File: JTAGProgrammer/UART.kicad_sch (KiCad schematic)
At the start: 25 parts, among them J3 Conn_01x06, U6 74LVC3G17, U7 74LVC3G17

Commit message: Add LCSC part numbers
Signed-off-by: Anthony Bernaert <anthony.bernaert@gmail.com>
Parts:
- D1: LCSC (none) -> C142698
- D4: LCSC (none) -> C324473
- J3: LCSC (none) -> C40877
- U6, U7: LCSC (none) -> C18213
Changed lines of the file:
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@@
+      (effects (font (size 1.27 1.27)) hide)
+    )
+    (property "LCSC" "C18213" (at 41.275 170.18 0)
       (effects (font (size 1.27 1.27)) hide)
     )
@@
       (effects (font (size 1.27 1.27)) (justify bottom) hide)
     )
+    (property "LCSC" "C142698" (at 197.485 87.63 90)
+      (effects (font (size 1.27 1.27)) hide)
+    )
     (pin "1")
     (pin "2")
@@
     )
     (property "Datasheet" "http://www.ti.com/lit/sg/scyt129e/scyt129e.pdf" (at 127.635 41.275 0)
+      (effects (font (size 1.27 1.27)) hide)
+    )
+    (property "LCSC" "C18213" (at 127.635 41.275 0)
       (effects (font (size 1.27 1.27)) hide)
     )
@@
       (effects (font (size 1.27 1.27)) hide)
     )
+    (property "LCSC" "C18213" (at 127.635 74.93 0)
+      (effects (font (size 1.27 1.27)) hide)
+    )
     (pin "1")
     (pin "7")
@@
       (effects (font (size 1.27 1.27)) hide)
     )
+    (property "LCSC" "C18213" (at 209.55 121.92 0)
+      (effects (font (size 1.27 1.27)) hide)
+    )
     (pin "1")
     (pin "7")
@@
       (effects (font (size 1.27 1.27)) hide)
     )
+    (property "LCSC" "C324473" (at 57.15 133.35 0)
+      (effects (font (size 1.27 1.27)) hide)
+    )
     (pin "1")
     (pin "2")
@@
     )
     (property "Datasheet" "~" (at 247.015 77.47 0)
+      (effects (font (size 1.27 1.27)) hide)
+    )
+    (property "LCSC" "C40877" (at 247.015 77.47 0)
       (effects (font (size 1.27 1.27)) hide)
     )
@@
       (effects (font (size 1.27 1.27)) hide)
     )
+    (property "LCSC" "C324473" (at 57.15 123.19 0)
+      (effects (font (size 1.27 1.27)) hide)
+    )
     (pin "1")
     (pin "2")
@@
     )
     (property "Datasheet" "http://www.ti.com/lit/sg/scyt129e/scyt129e.pdf" (at 64.77 170.18 0)
+      (effects (font (size 1.27 1.27)) hide)
+    )
+    (property "LCSC" "C18213" (at 64.77 170.18 0)
       (effects (font (size 1.27 1.27)) hide)
     )
@@
       (effects (font (size 1.27 1.27)) hide)
     )
+    (property "LCSC" "C18213" (at 209.55 142.875 0)
+      (effects (font (size 1.27 1.27)) hide)
+    )
     (pin "1")
     (pin "7")
@@
       (effects (font (size 1.27 1.27)) (justify bottom) hide)
     )
+    (property "LCSC" "C142698" (at 210.185 87.63 90)
+      (effects (font (size 1.27 1.27)) hide)
+    )
     (pin "1")
     (pin "2")
@@
     )
     (property "Datasheet" "http://www.ti.com/lit/sg/scyt129e/scyt129e.pdf" (at 125.095 92.71 0)
+      (effects (font (size 1.27 1.27)) hide)
+    )
+    (property "LCSC" "C18213" (at 125.095 92.71 0)
       (effects (font (size 1.27 1.27)) hide)
     )
@@
       (effects (font (size 1.27 1.27)) hide)
     )
+    (property "LCSC" "C324473" (at 57.15 113.03 0)
+      (effects (font (size 1.27 1.27)) hide)
+    )
     (pin "1")
     (pin "2")
@@
       (effects (font (size 1.27 1.27)) (justify bottom) hide)
     )
+    (property "LCSC" "C142698" (at 203.835 87.63 90)
+      (effects (font (size 1.27 1.27)) hide)
+    )
     (pin "1")
     (pin "2")
@@
       (effects (font (size 1.27 1.27)) (justify bottom) hide)
     )
+    (property "LCSC" "C142698" (at 216.535 87.63 90)
+      (effects (font (size 1.27 1.27)) hide)
+    )
     (pin "1")
     (pin "2")
@@
       (effects (font (size 1.27 1.27)) hide)
     )
+    (property "LCSC" "C18213" (at 125.73 58.42 0)
+      (effects (font (size 1.27 1.27)) hide)
+    )

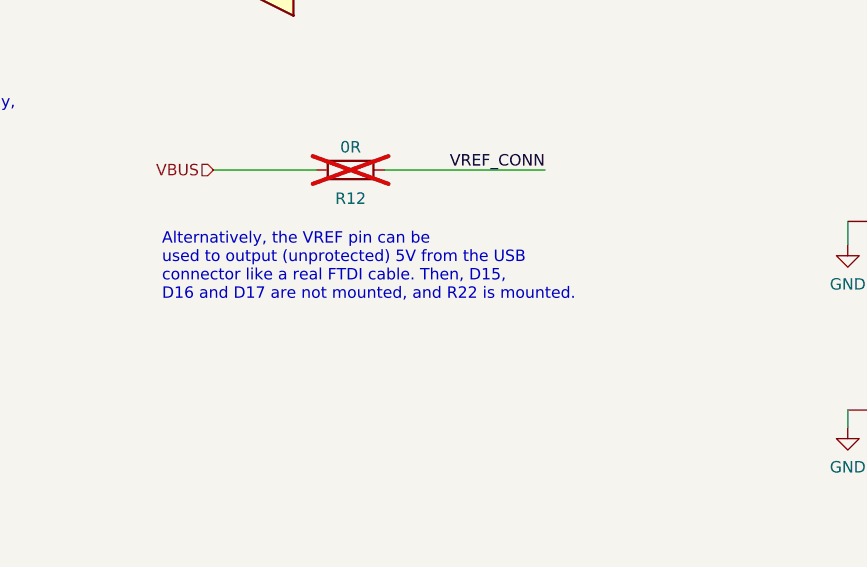
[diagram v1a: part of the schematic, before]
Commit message: Fix wrong comment in schematic on UART VREF/5V mounting options
Signed-off-by: Anthony Bernaert <anthony.bernaert@gmail.com>
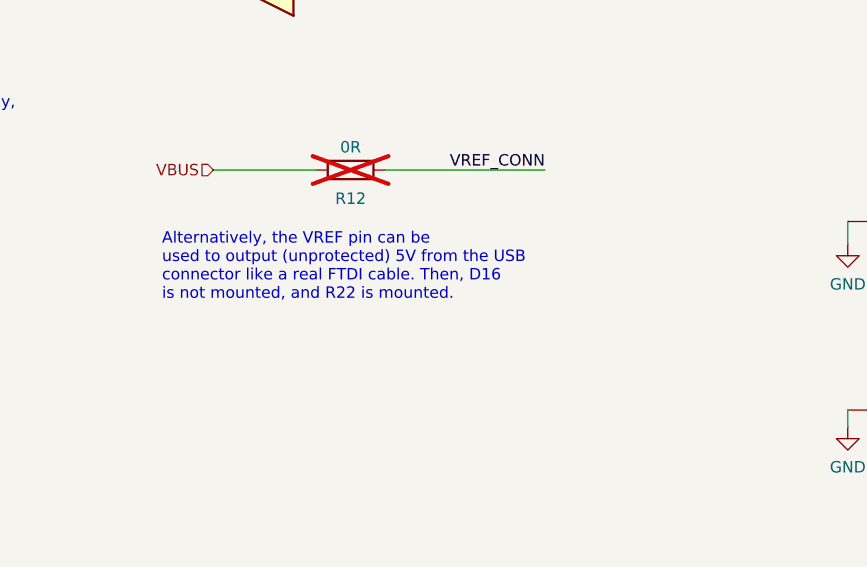
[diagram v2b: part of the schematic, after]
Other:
- note added: "Alternatively, the VREF pin can be used to output (unprotected) 5V from the USB connector like a real FTDI cable. Then, D16 is not mounted, and R22 is mounted."
- note removed: "Alternatively, the VREF pin can be used to output (unprotected) 5V from the USB connector like a real FTDI cable. Then, D15, D16 and D17 are not mounted, and R22 is mounted."
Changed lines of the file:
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@@
     (title "FTDI JTAG Programmer")
     (date "2024-10-11")
-    (rev "1")
+    (rev "1.1")
   )
   (junction (at 210.185 92.71) (diameter 0) (color 0 0 0 0)
@@
     (stroke (width 0) (type default))
   )
-  (text "Alternatively, the VREF pin can be \nused to output (unprotected) 5V from the USB\nconnector like a real FTDI cable. Then, D15,\nD16 and D17 are not mounted, and R22 is mounted."
+  (text "Alternatively, the VREF pin can be \nused to output (unprotected) 5V from the USB\nconnector like a real FTDI cable. Then, D16\nis not mounted, and R22 is mounted."
     (at 118.11 130.81 0)
     (effects (font (size 1.27 1.27)) (justify left bottom))

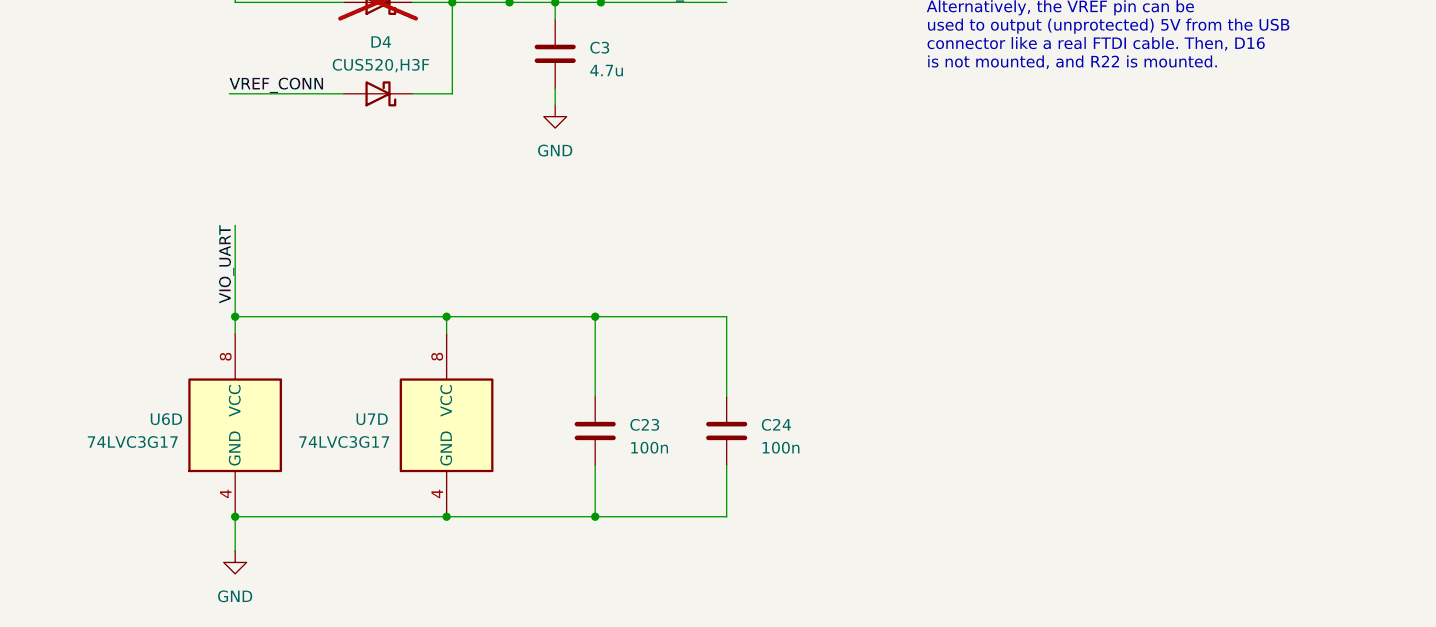
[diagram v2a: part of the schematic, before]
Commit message: Rev.2: change to USB Type-C, add VBUS fuse, VREF LED indicators
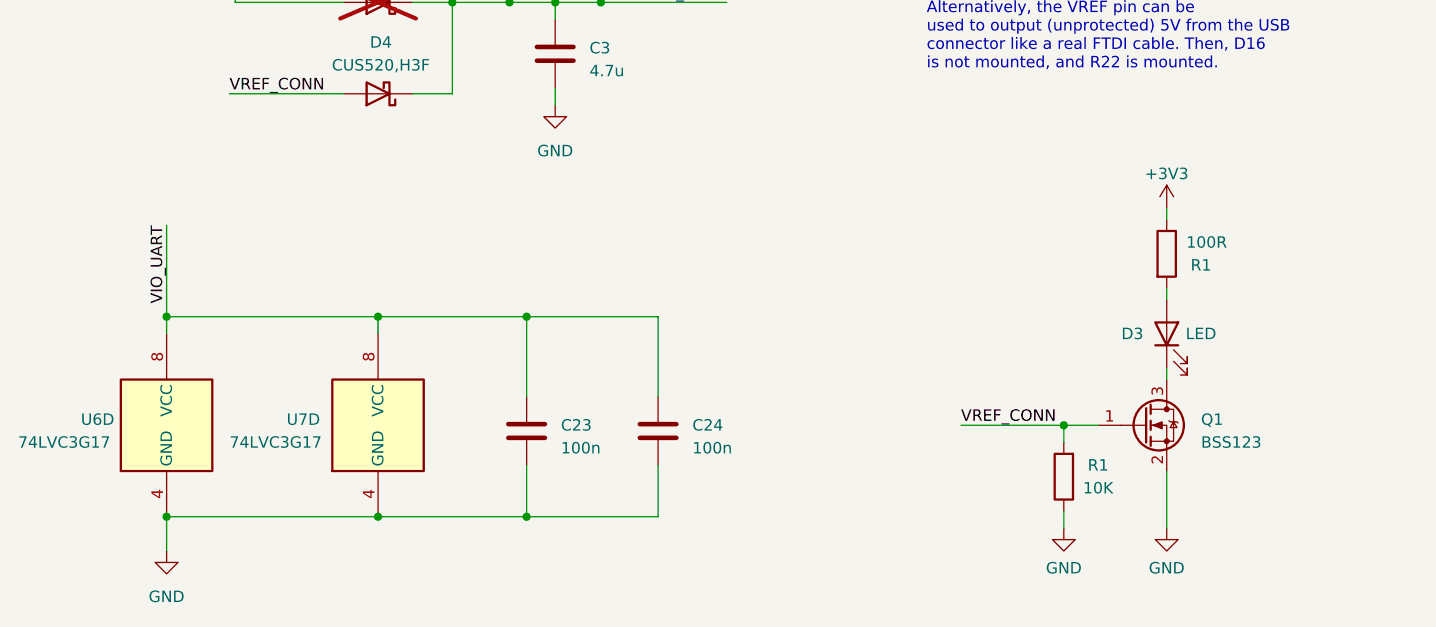
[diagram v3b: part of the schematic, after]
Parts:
- added D3: LED, LED_SMD:LED_0603_1608Metric, symbol Device:LED
- added Q1: BSS123, Package_TO_SOT_SMD:SOT-23, symbol Transistor_FET:BSS123
- added R1: 100R, Resistor_SMD:R_0603_1608Metric, symbol Device:R
- added R1: 10K, Resistor_SMD:R_0603_1608Metric, symbol Device:R
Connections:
- net +3V3: now also R1.1
- net GND: now also Q1.2 (S), R1.1
- net VREF_CONN: now also Q1.1 (G), R1.2
- new net: D3.1 (K), Q1.3 (D)
- new net: D3.2 (A), R1.2
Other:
- moved on the sheet: C23, C24, U6D, U7D
